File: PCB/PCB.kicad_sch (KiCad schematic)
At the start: 120 parts, among them J1 SS-53000-003, U1 Hx711, U10 Hx711, U11 Hx711, U12 Hx711, U13 LT3042xMSE, U2 Hx711, U3 Hx711, U4 Hx711, U5 Hx711, U6 Hx711, U7 Hx711, U8 Hx711, U9 Hx711

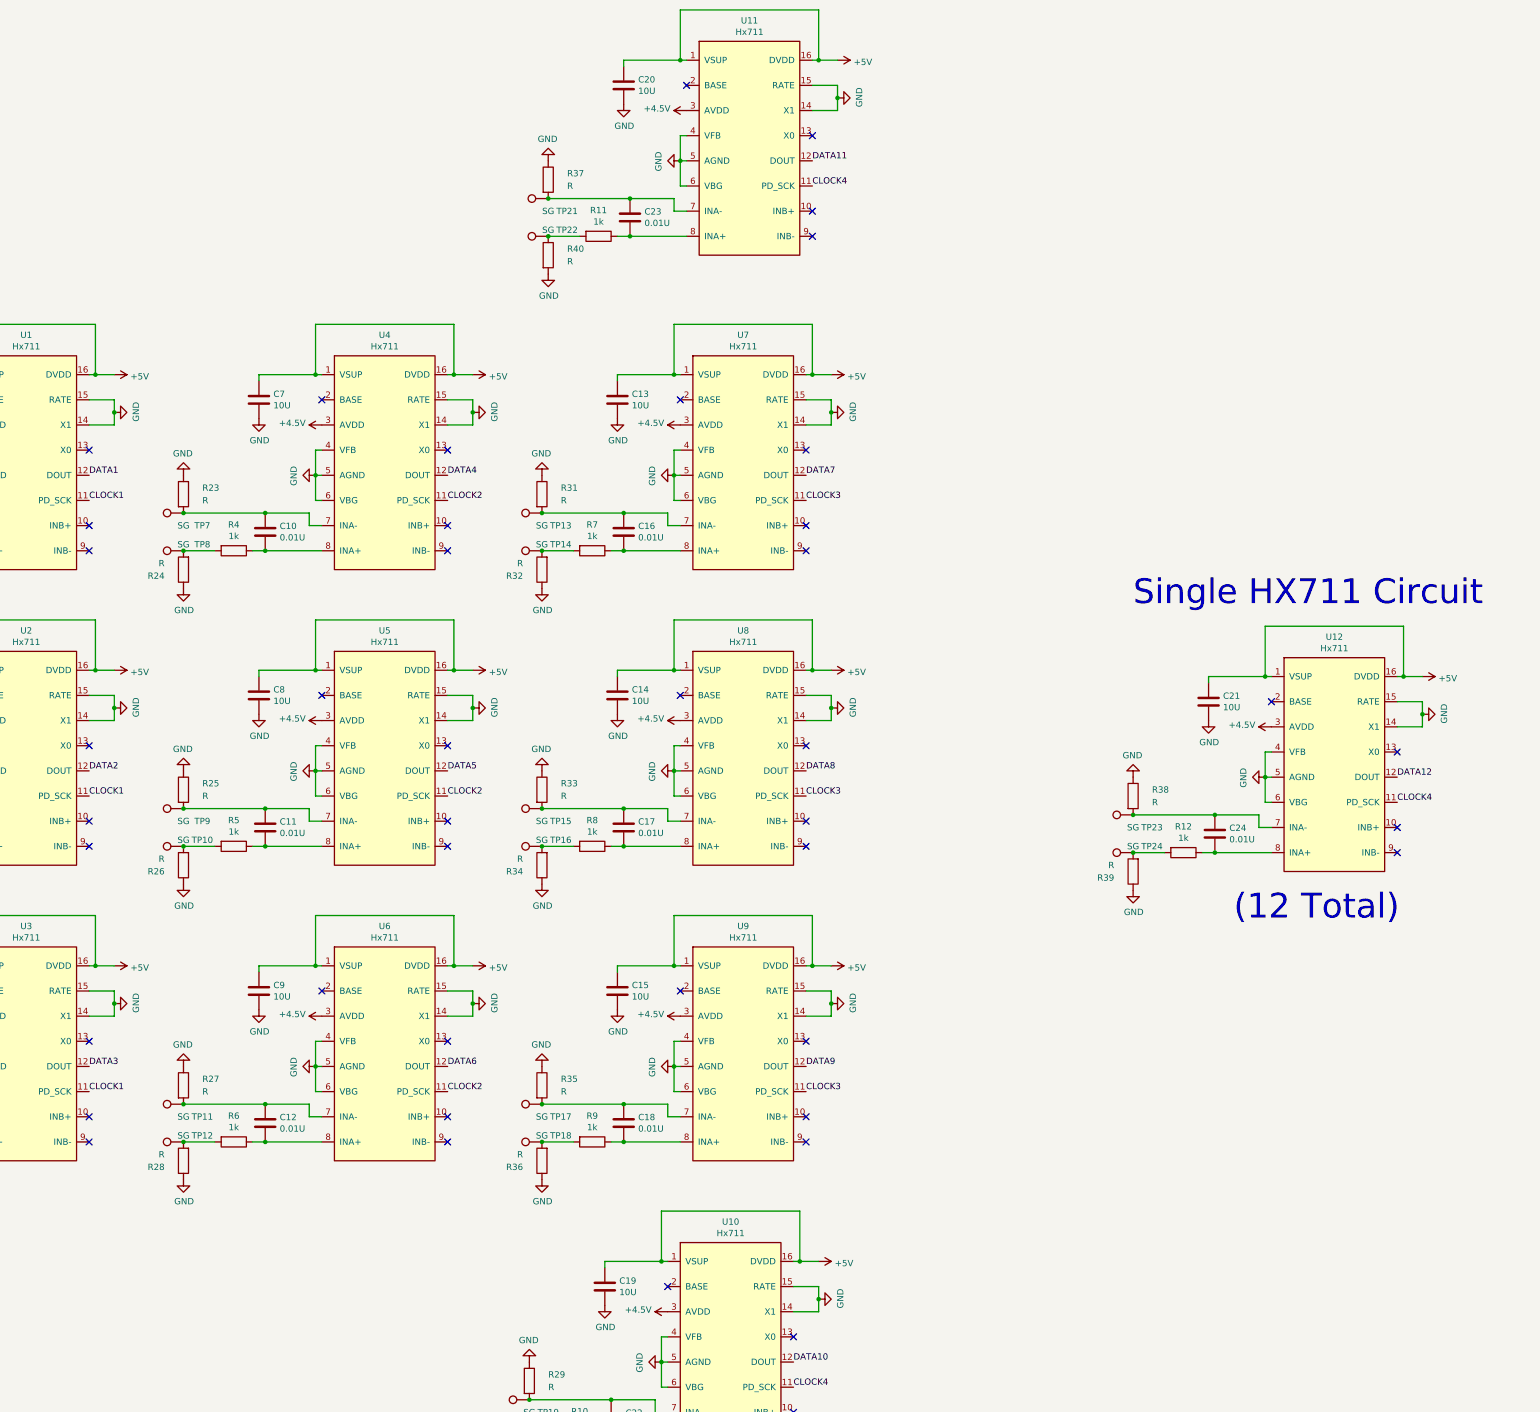
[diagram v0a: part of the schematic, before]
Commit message: Set RATE high for 80hz
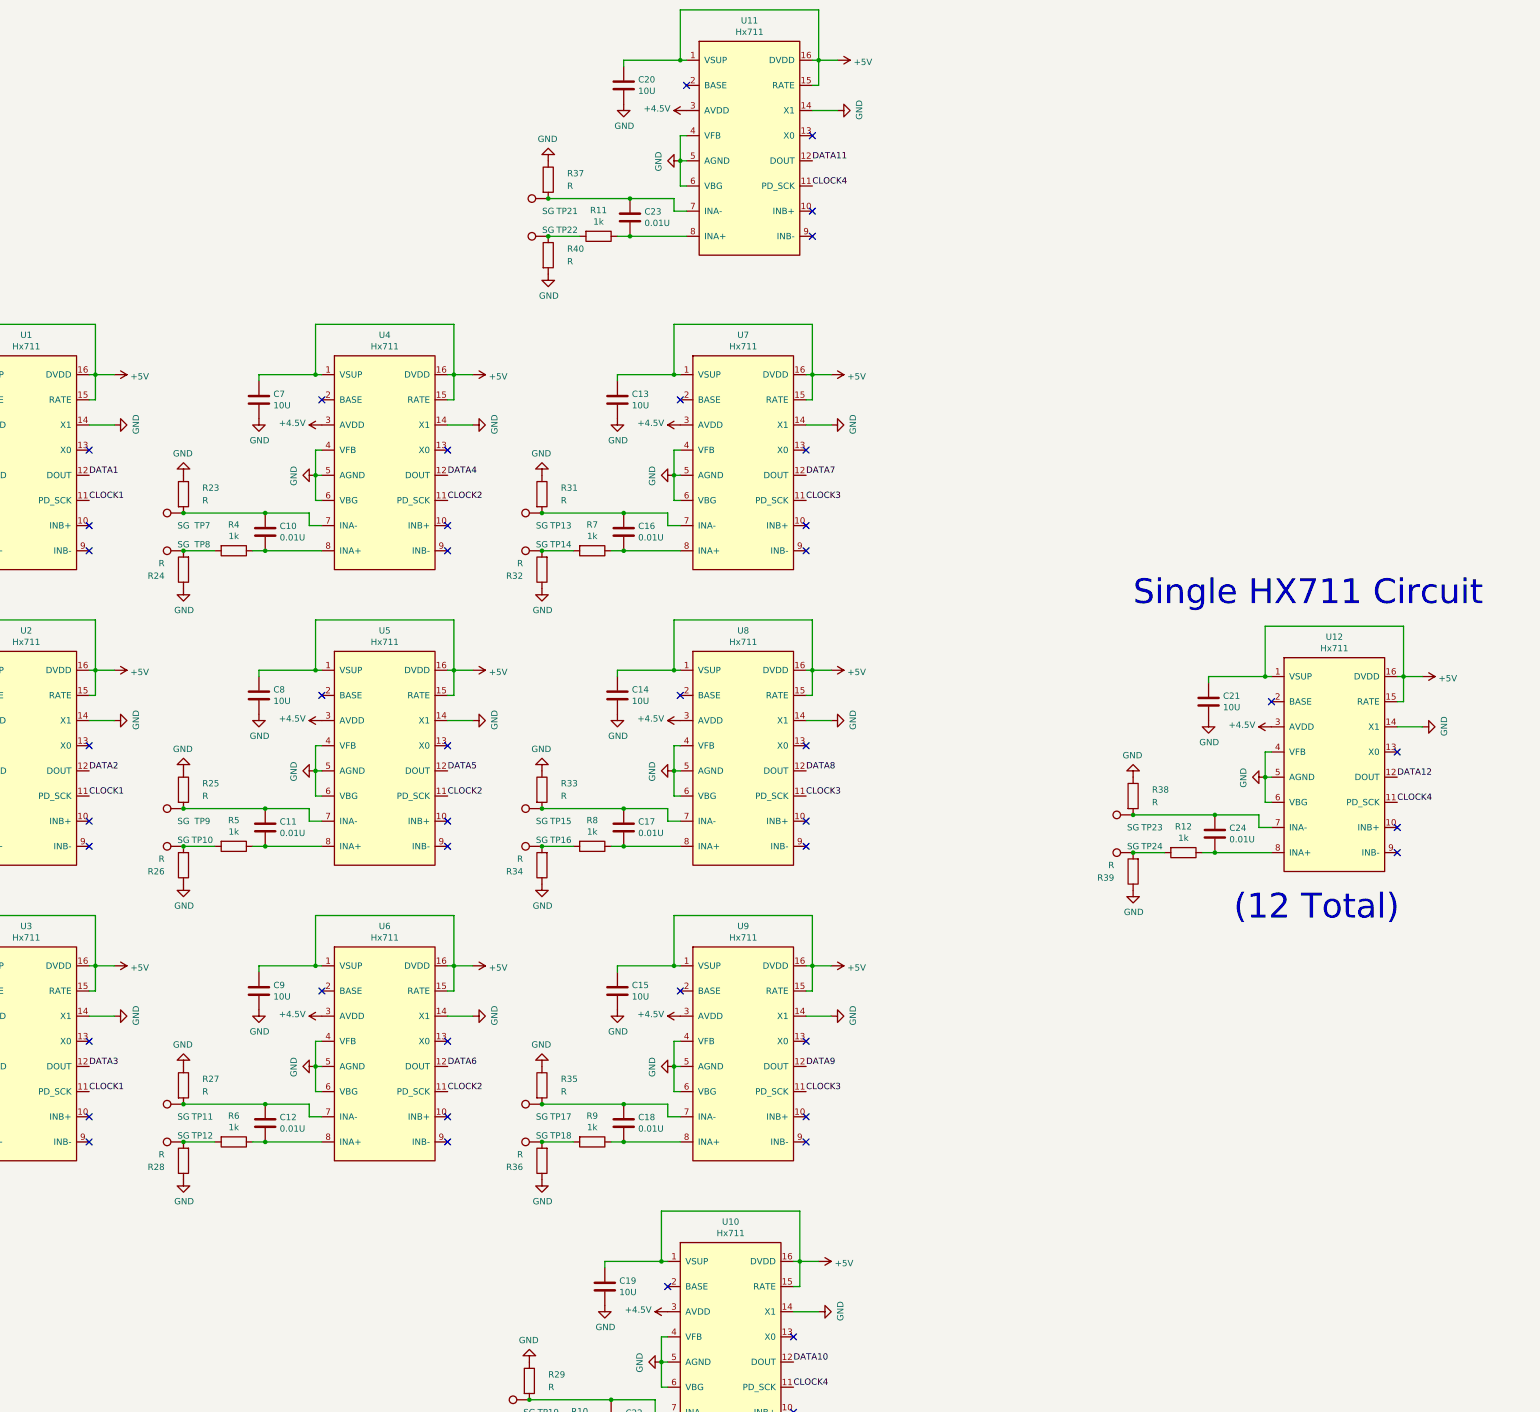
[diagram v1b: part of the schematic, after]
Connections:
- net +5V: now also U1.15 (RATE), U10.15 (RATE), U11.15 (RATE), U12.15 (RATE), U2.15 (RATE), U3.15 (RATE), U4.15 (RATE), U5.15 (RATE), U6.15 (RATE), U7.15 (RATE), U8.15 (RATE), U9.15 (RATE)
- net GND: no longer U1.15 (RATE), U10.15 (RATE), U11.15 (RATE), U12.15 (RATE), U2.15 (RATE), U3.15 (RATE), U4.15 (RATE), U5.15 (RATE), U6.15 (RATE), U7.15 (RATE), U8.15 (RATE), U9.15 (RATE)

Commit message: Add hierachial and shift registers
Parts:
- removed C1, C13, C14, C15, C19, C2, C20, C21, C3, C7, C8, C9: 10U, Capacitor_SMD:C_0805_2012Metric_Pad1.18x1.45mm_HandSolder, symbol PCB-rescue:C-Device
- removed C10, C11, C12, C16, C17, C18, C22, C23, C24, C4, C5, C6: 0.01U, Capacitor_SMD:C_0805_2012Metric_Pad1.18x1.45mm_HandSolder, symbol PCB-rescue:C-Device
- removed J1: SS-53000-003, SS-53000-003:BEL_SS-53000-003, symbol SS-53000-003:SS-53000-003
- removed JP1, JP2, JP3: SolderJumper_2_Open, Jumper:SolderJumper-2_P1.3mm_Open_Pad1.0x1.5mm, symbol Jumper:SolderJumper_2_Open
- removed R1, R10, R11, R12, R2, R3, R4, R5, R6, R7, R8, R9: 1k, Resistor_SMD:R_0805_2012Metric_Pad1.20x1.40mm_HandSolder, symbol PCB-rescue:R-Device
- removed R17, R18, R19, R20, R21, R22, R23, R24, R25, R26, R27, R28, R29, R30, R31, R32, R33, R34, R35, R36, R37, R38, R39, R40: R, Resistor_SMD:R_0805_2012Metric_Pad1.20x1.40mm_HandSolder, symbol Device:R
- removed TP1, TP10, TP11, TP12, TP13, TP14, TP15, TP16, TP17, TP18, TP19, TP2, TP20, TP21, TP22, TP23, TP24, TP3, TP4, TP5, TP6, TP7, TP8, TP9: SG, Custom-footprints:Radial-Pads-With-Relief, symbol PCB-rescue:TestPoint-Connector
- removed TP28, TP29, TP30: GND, Custom-footprints:Radial-Pads-With-Relief, symbol PCB-rescue:TestPoint-Connector
- removed U1, U10, U11, U12, U2, U3, U4, U5, U6, U7, U8, U9: Hx711, Package_SO:SOIC-16_3.9x9.9mm_P1.27mm, symbol PCB-rescue:Hx711-HX711-HX711-ADC-rescue
- added J?: (no value), symbol Connector:Conn_01x06_Female
- added U? (x2): SN74HC165N, digikey-footprints:DIP-16_W7.62mm, symbol dk_Logic-Shift-Registers:SN74HC165N
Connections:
- net +5V: now also J?.5 (Pin_5), U?.16 (VCC), U?.16 (VCC)
- net GND: now also J?.6 (Pin_6), U?.8 (GND), U?.8 (GND)
- net +4V renamed 4.5V
- new net: U?.10 (SER), U?.9 (QH)
- new net DATA: J?.2 (Pin_2), U?.9 (QH)
- new net HX711 Circuit/DOUT: U?.5 (G)
- new net HX711 Circuit1/DOUT: U?.6 (H)
- new net HX711 Circuit10/DOUT: U?.14 (D)
- new net HX711 Circuit11/DOUT: U?.13 (C)
- new net HX711 Circuit12/DOUT: U?.4 (F)
- new net HX711 Circuit13/DOUT: U?.12 (B)
- new net HX711 Circuit14/DOUT: U?.11 (A)
- new net HX711 Circuit2/DOUT: U?.11 (A)
- new net HX711 Circuit3/DOUT: U?.12 (B)
- new net HX711 Circuit4/DOUT: U?.13 (C)
- new net HX711 Circuit5/DOUT: U?.14 (D)
- new net HX711 Circuit9/DOUT: U?.3 (E)
- new net HX_CLK: J?.4 (Pin_4)
- new net LOAD: J?.3 (Pin_3), U?.1 (SH/~{LD}), U?.1 (SH/~{LD})
- new net S_CLK: J?.1 (Pin_1), U?.2 (CLK), U?.2 (CLK)
- no-connect marks 48 -> 0
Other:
- added sheet HX711 Circuit (HX711 Circuit.kicad_sch)
- added sheet HX711 Circuit1 (HX711 Circuit.kicad_sch)
- added sheet HX711 Circuit10 (HX711 Circuit.kicad_sch)
- added sheet HX711 Circuit11 (HX711 Circuit.kicad_sch)
- added sheet HX711 Circuit12 (HX711 Circuit.kicad_sch)
- added sheet HX711 Circuit13 (HX711 Circuit.kicad_sch)
- added sheet HX711 Circuit14 (HX711 Circuit.kicad_sch)
- added sheet HX711 Circuit2 (HX711 Circuit.kicad_sch)
- added sheet HX711 Circuit3 (HX711 Circuit.kicad_sch)
- added sheet HX711 Circuit4 (HX711 Circuit.kicad_sch)
- added sheet HX711 Circuit5 (HX711 Circuit.kicad_sch)
- added sheet HX711 Circuit9 (HX711 Circuit.kicad_sch)
- note added: "12 HX711 Sensors"
- note added: "Data is read from HX711s into shift registers using HX_CLK and LOAD. Shift registers are clocked using S_CLK and data is shifted out on DATA to flight computer."
- note added: "Regulated output for strain gauges"
- note removed: "(12 Total)"
- note removed: "Clock Jumper (Short to save GPIO)"
- note removed: "Female HDMI"
- note removed: "Single HX711 Circuit"
- moved on the sheet: C25, C26, C27, H1, H2, H3, H4, H5, LD1, R13, R14, R15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

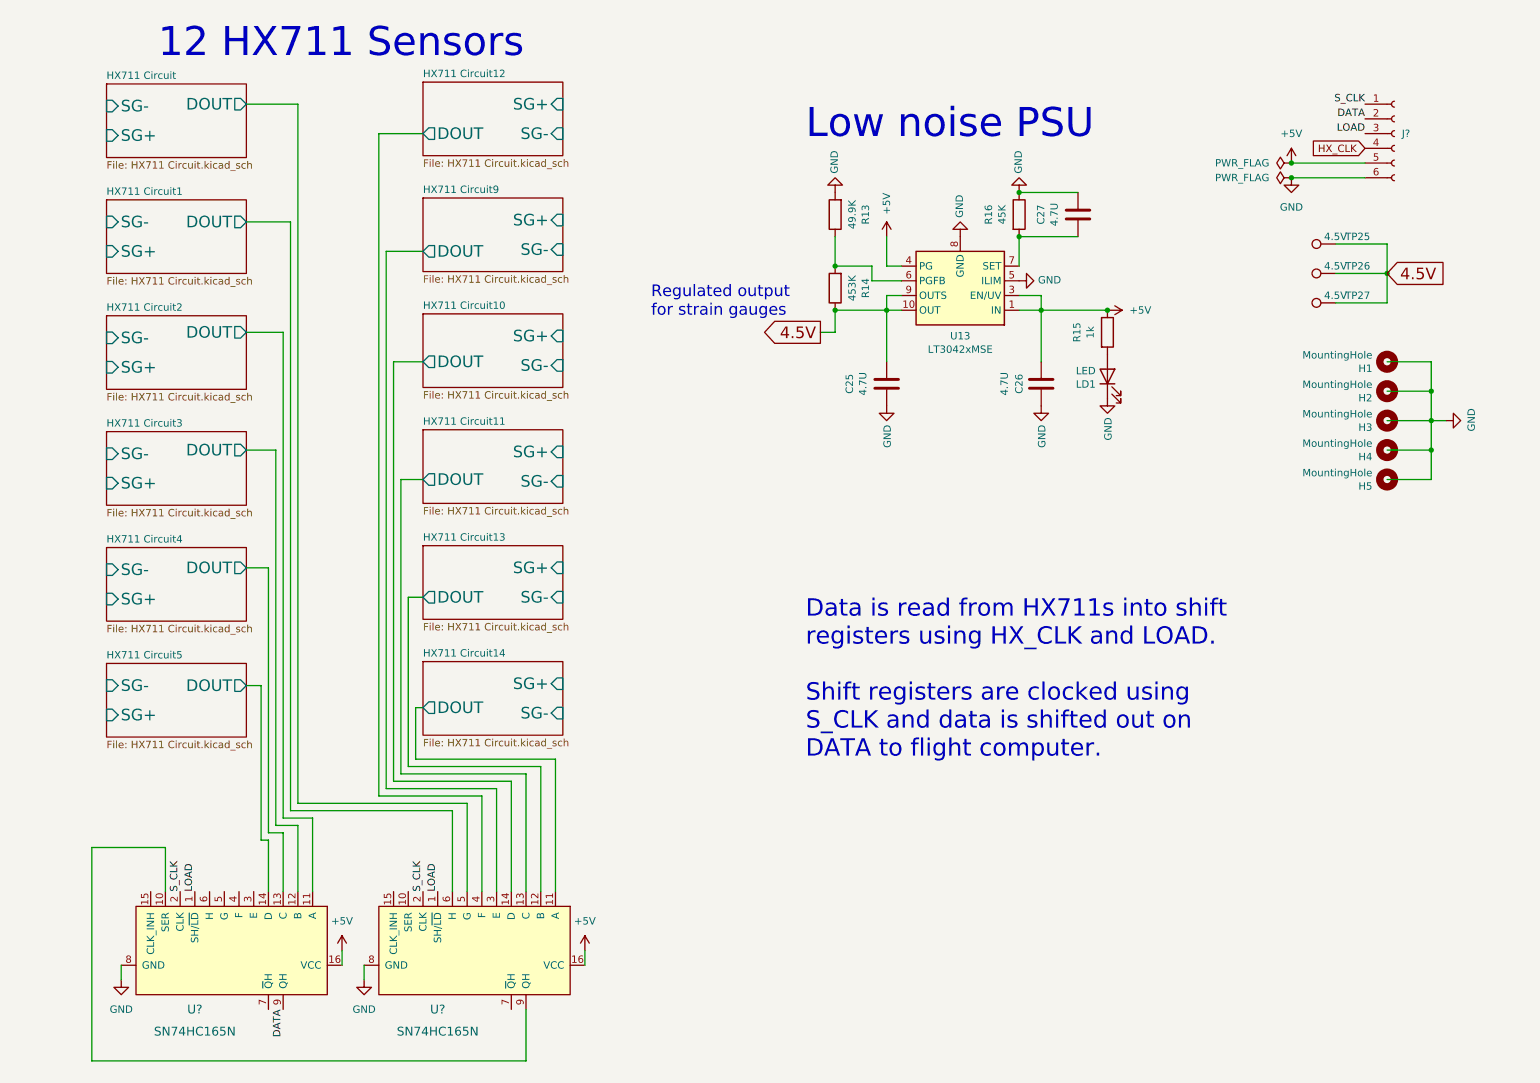
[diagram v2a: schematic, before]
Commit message: Swap shift registers. Start board layout
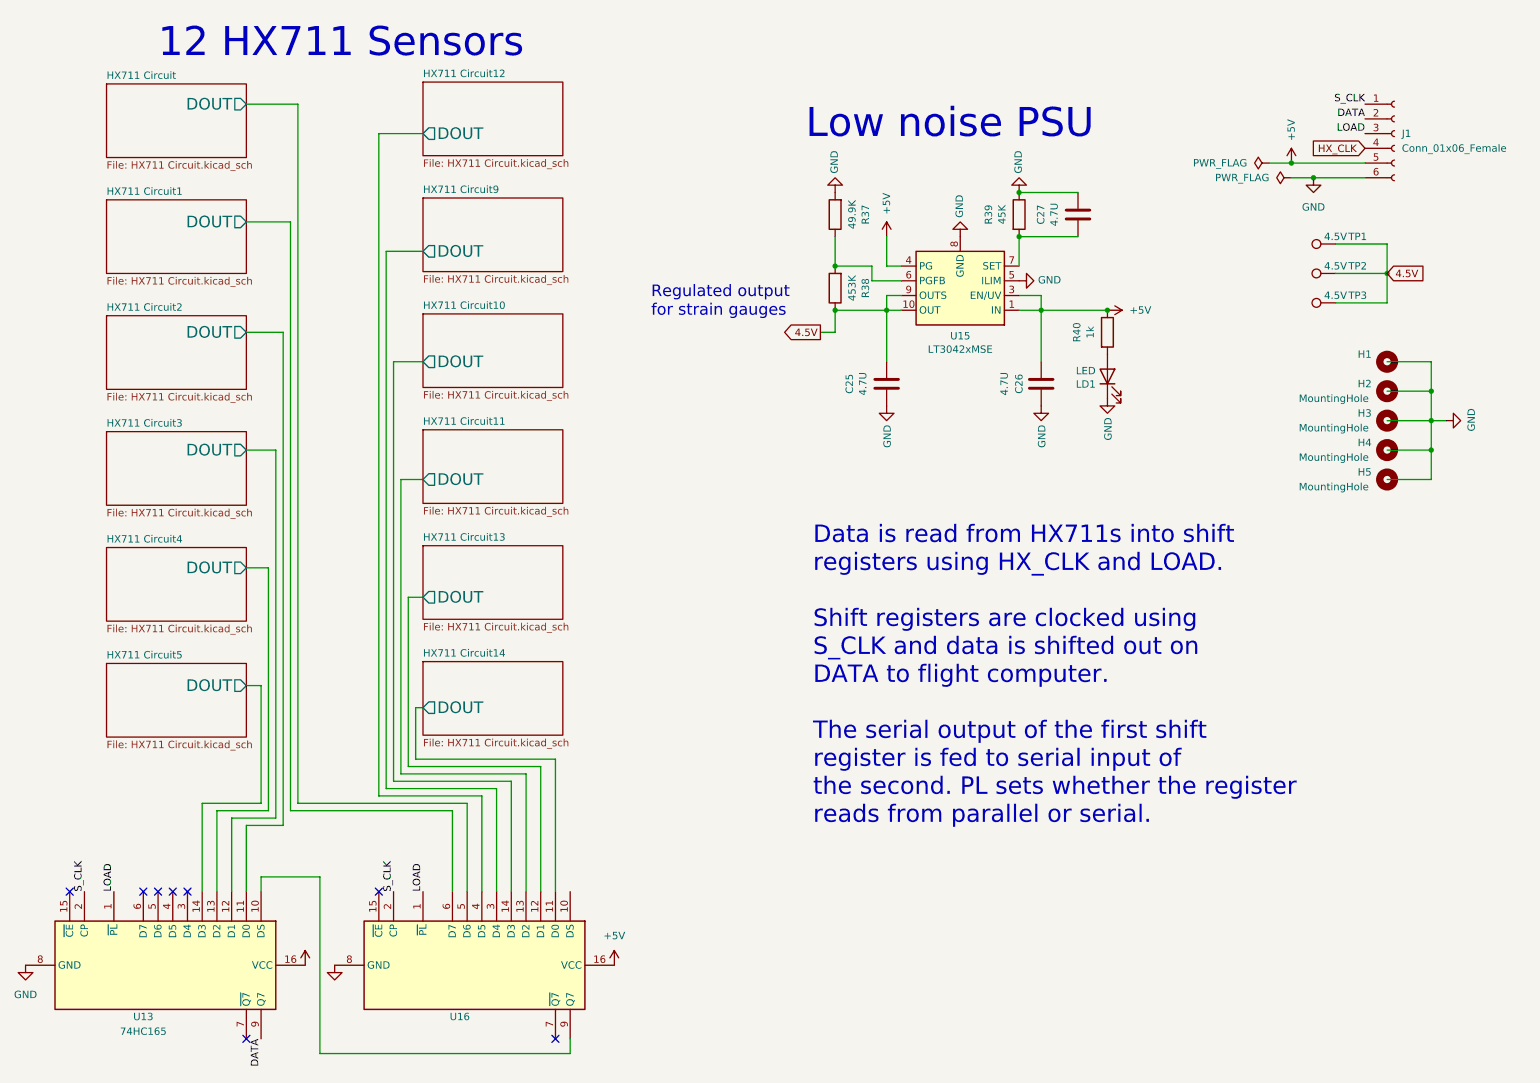
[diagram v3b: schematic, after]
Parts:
- removed H1, H2, H3, H4: MountingHole, MountingHole:MountingHole_3.7mm_Pad_TopBottom, symbol PCB-rescue:MountingHole-Mechanical
- removed H5: MountingHole, MountingHole:MountingHole_6.4mm_M6, symbol PCB-rescue:MountingHole-Mechanical
- removed U? (x2): SN74HC165N, digikey-footprints:DIP-16_W7.62mm, symbol dk_Logic-Shift-Registers:SN74HC165N
- added H1: (no value), symbol Mechanical:MountingHole
- added H2, H3, H4, H5: MountingHole, symbol Mechanical:MountingHole
- added U13: 74HC165, Package_SO:SO-16_3.9x9.9mm_P1.27mm, symbol 74xx:74HC165
- added U16: (no value), symbol 74xx:74HC165
- J1: renamed from J?; value (none) -> Conn_01x06_Female
- renumbered R13 to R37, R14 to R38, R16 to R39, R15 to R40, TP25 to TP1, TP26 to TP2, TP27 to TP3, U13 to U15
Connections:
- net +5V: now also U13.16 (VCC), U16.16 (VCC)
- net DATA: now also U13.9 (Q7)
- net GND: now also U13.8 (GND), U16.8 (GND)
- net HX711 Circuit/DOUT: now also U16.5 (D6)
- net HX711 Circuit1/DOUT: now also U16.6 (D7)
- net HX711 Circuit10/DOUT: now also U16.14 (D3)
- net HX711 Circuit11/DOUT: now also U16.13 (D2)
- net HX711 Circuit12/DOUT: now also U16.4 (D5)
- net HX711 Circuit13/DOUT: now also U16.12 (D1)
- net HX711 Circuit14/DOUT: now also U16.11 (D0)
- net HX711 Circuit2/DOUT: now also U13.11 (D0)
- net HX711 Circuit3/DOUT: now also U13.12 (D1)
- net HX711 Circuit4/DOUT: now also U13.13 (D2)
- net HX711 Circuit5/DOUT: now also U13.14 (D3)
- net HX711 Circuit9/DOUT: now also U16.3 (D4)
- net LOAD: now also U13.1 (~{PL}), U16.1 (~{PL})
- net S_CLK: now also U13.2 (CP), U16.2 (CP)
- new net: U13.10 (DS), U16.9 (Q7)
- no-connect marks 0 -> 8
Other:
- sheet HX711 Circuit ports: added none; removed SG+, SG-
- sheet HX711 Circuit1 ports: added none; removed SG+, SG-
- sheet HX711 Circuit10 ports: added none; removed SG+, SG-
- sheet HX711 Circuit11 ports: added none; removed SG+, SG-
- sheet HX711 Circuit12 ports: added none; removed SG+, SG-
- sheet HX711 Circuit13 ports: added none; removed SG+, SG-
- sheet HX711 Circuit14 ports: added none; removed SG+, SG-
- sheet HX711 Circuit2 ports: added none; removed SG+, SG-
- sheet HX711 Circuit3 ports: added none; removed SG+, SG-
- sheet HX711 Circuit4 ports: added none; removed SG+, SG-
- sheet HX711 Circuit5 ports: added none; removed SG+, SG-
- sheet HX711 Circuit9 ports: added none; removed SG+, SG-
- note added: "Data is read from HX711s into shift registers using HX_CLK and LOAD. Shift registers are clocked using S_CLK and data is shifted out on DATA to flight computer. The serial output of the first shift register is fed to serial input of the second. PL sets whether the register reads from parallel or serial."
- note removed: "Data is read from HX711s into shift registers using HX_CLK and LOAD. Shift registers are clocked using S_CLK and data is shifted out on DATA to flight computer."
